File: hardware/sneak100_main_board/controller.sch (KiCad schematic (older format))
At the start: 17 parts, among them U7 STM32F405RGTx, Y1 8MHz

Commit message: Hardware configuration schematic
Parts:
- added R24, R25: 4k7, Resistor_SMD:R_0805_2012Metric, symbol Device:R
- renumbered C13 to C14, C14 to C15, C15 to C16, C16 to C17, C17 to C18, C18 to C19, C19 to C20, C20 to C21, C21 to C22, C22 to C23, C23 to C24, C24 to C25, R19 to R23, U7 to U8
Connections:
- net +3V3: now also R24.1, R25.1
- net LINE_RM: now reaches U8.10 (PC2)
- net LINE_RR: now reaches U8.11 (PC3)
- net RF_A: now reaches U8.14 (PA0)
- net RF_B: now reaches U8.15 (PA1)
- net USART2_TX: now reaches U8.16 (PA2)
- net USART2_RX: now reaches U8.17 (PA3)
- net MODULE_START: now reaches U8.2 (PC13)
- net LB_A: now reaches U8.22 (PA6)
- net LB_B: now reaches U8.23 (PA7)
- net BATTERY_SENSE: now reaches U8.24 (PC4)
- net PROXIMITY_RX_READ: now reaches U8.25 (PC5)
- net LB_IN1: now reaches U8.26 (PB0)
- net LB_IN2: now reaches U8.27 (PB1)
- net RF_IN1: now reaches U8.29 (PB10)
- net MODULE_KILL: now reaches U8.3 (PC14)
- net RF_IN2: now reaches U8.30 (PB11)
- net LF_IN1: now reaches U8.35 (PB14)
- net LF_IN2: now reaches U8.36 (PB15)
- net LF_A: now reaches U8.37 (PC6)
- net LF_B: now reaches U8.38 (PC7)
- net PROXIMITY_TX_ENABLE: now reaches U8.39 (PC8)
- net I2C3_SDA: now reaches U8.40 (PC9)
- net I2C3_SDA: now also R25.2
- net I2C3_SCL: now reaches U8.41 (PA8)
- net I2C3_SCL: now also R24.2
- net USB_DM: now reaches U8.44 (PA11)
- net USB_DP: now reaches U8.45 (PA12)
- net USER_LED1: now reaches U8.50 (PA15)
- net USER_LED2: now reaches U8.51 (PC10)
- net USER_LED3: now reaches U8.52 (PC11)
- net USER_BUTTON: now reaches U8.53 (PC12)
- net RECEIVER_OUT: now reaches U8.54 (PD2)
- net PROXIMITY_ADD0: now reaches U8.55 (PB3)
- net PROXIMITY_ADD1: now reaches U8.56 (PB4)
- net PROXIMITY_ADD2: now reaches U8.57 (PB5)
- net RB_A: now reaches U8.58 (PB6)
- net RB_B: now reaches U8.59 (PB7)
- net RB_IN1: now reaches U8.61 (PB8)
- net RB_IN2: now reaches U8.62 (PB9)
- net LINE_LL: now reaches U8.8 (PC0)
- net LINE_LM: now reaches U8.9 (PC1)
- no-connect marks 3 -> 11

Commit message: Power section scheme
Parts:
- C18: renamed from C14; footprint Capacitor_SMD:C_0805_2012Metric -> Capacitor_SMD:C_0603_1608Metric
- C19: renamed from C15; footprint Capacitor_SMD:C_0805_2012Metric -> Capacitor_SMD:C_0603_1608Metric
- C20: renamed from C16; footprint Capacitor_SMD:C_0805_2012Metric -> Capacitor_SMD:C_0603_1608Metric
- C21: renamed from C17; footprint Capacitor_SMD:C_0805_2012Metric -> Capacitor_SMD:C_0603_1608Metric
- C22: renamed from C18; footprint Capacitor_SMD:C_0805_2012Metric -> Capacitor_SMD:C_0603_1608Metric
- C23: renamed from C19; footprint Capacitor_SMD:C_0805_2012Metric -> Capacitor_SMD:C_0603_1608Metric
- C24: renamed from C20; footprint Capacitor_SMD:C_0805_2012Metric -> Capacitor_SMD:C_0603_1608Metric
- C25: renamed from C21; footprint Capacitor_SMD:C_0805_2012Metric -> Capacitor_SMD:C_0603_1608Metric
- C26: renamed from C22; footprint Capacitor_SMD:C_0805_2012Metric -> Capacitor_SMD:C_0603_1608Metric
- C27: renamed from C23; footprint Capacitor_SMD:C_0805_2012Metric -> Capacitor_SMD:C_0603_1608Metric
- C28: renamed from C24; footprint Capacitor_SMD:C_0805_2012Metric -> Capacitor_SMD:C_0603_1608Metric
- renumbered C25 to C29, R23 to R32, R24 to R33, R25 to R34, U8 to U9

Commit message: USB FDU mode
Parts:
- added R19: 4k7, Resistor_SMD:R_0603_1608Metric, symbol Device:R
- added SW2: SW_SPST, Button_Switch_THT:SW_DIP_SPSTx01_Slide_9.78x4.72mm_W7.62mm_P2.54mm, symbol Switch:SW_SPST
- added SW5: SW_Push, Button_Switch_SMD:SW_SPST_FSMSM, symbol Switch:SW_Push
- R20: renamed from R32; value 10k -> 4k7; footprint Resistor_SMD:R_0805_2012Metric -> Resistor_SMD:R_0603_1608Metric
- R21: renamed from R33; footprint Resistor_SMD:R_0805_2012Metric -> Resistor_SMD:R_0603_1608Metric
- R22: renamed from R34; footprint Resistor_SMD:R_0805_2012Metric -> Resistor_SMD:R_0603_1608Metric
- renumbered C18 to C16, C19 to C17, C20 to C18, C21 to C19, C22 to C20, C23 to C21, C24 to C22, C25 to C23, C26 to C24, C27 to C25, C28 to C26, C29 to C27, U9 to U8
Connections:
- net labels added: BOOT0, BOOT1
- wire segments 37 -> 46
- no-connect marks 11 -> 10

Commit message: Layout progress
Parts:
- removed C16: 100nF, Capacitor_SMD:C_0603_1608Metric, symbol Device:C
- removed SW2: SW_SPST, Button_Switch_THT:SW_DIP_SPSTx01_Slide_9.78x4.72mm_W7.62mm_P2.54mm, symbol Switch:SW_SPST
- removed SW5: SW_Push, Button_Switch_SMD:SW_SPST_FSMSM, symbol Switch:SW_Push
- added J14: Conn_02x02_Odd_Even, Connector_PinHeader_2.54mm:PinHeader_2x02_P2.54mm_Vertical, symbol Connector_Generic:Conn_02x02_Odd_Even
- renumbered C17 to C18, C18 to C19, C19 to C20, C20 to C21, C21 to C22, C22 to C23, C23 to C24, C24 to C25, C25 to C26, C26 to C27, C27 to C28, R19 to R27, R20 to R28, R21 to R29, R22 to R30, U8 to U9
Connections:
- net labels added: RST, ST-LINK_3.3V
- net labels removed: MODULE_KILL, MODULE_START, RESET
- wire segments 46 -> 40
- no-connect marks 10 -> 12
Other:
- moved on the sheet: R27, R28

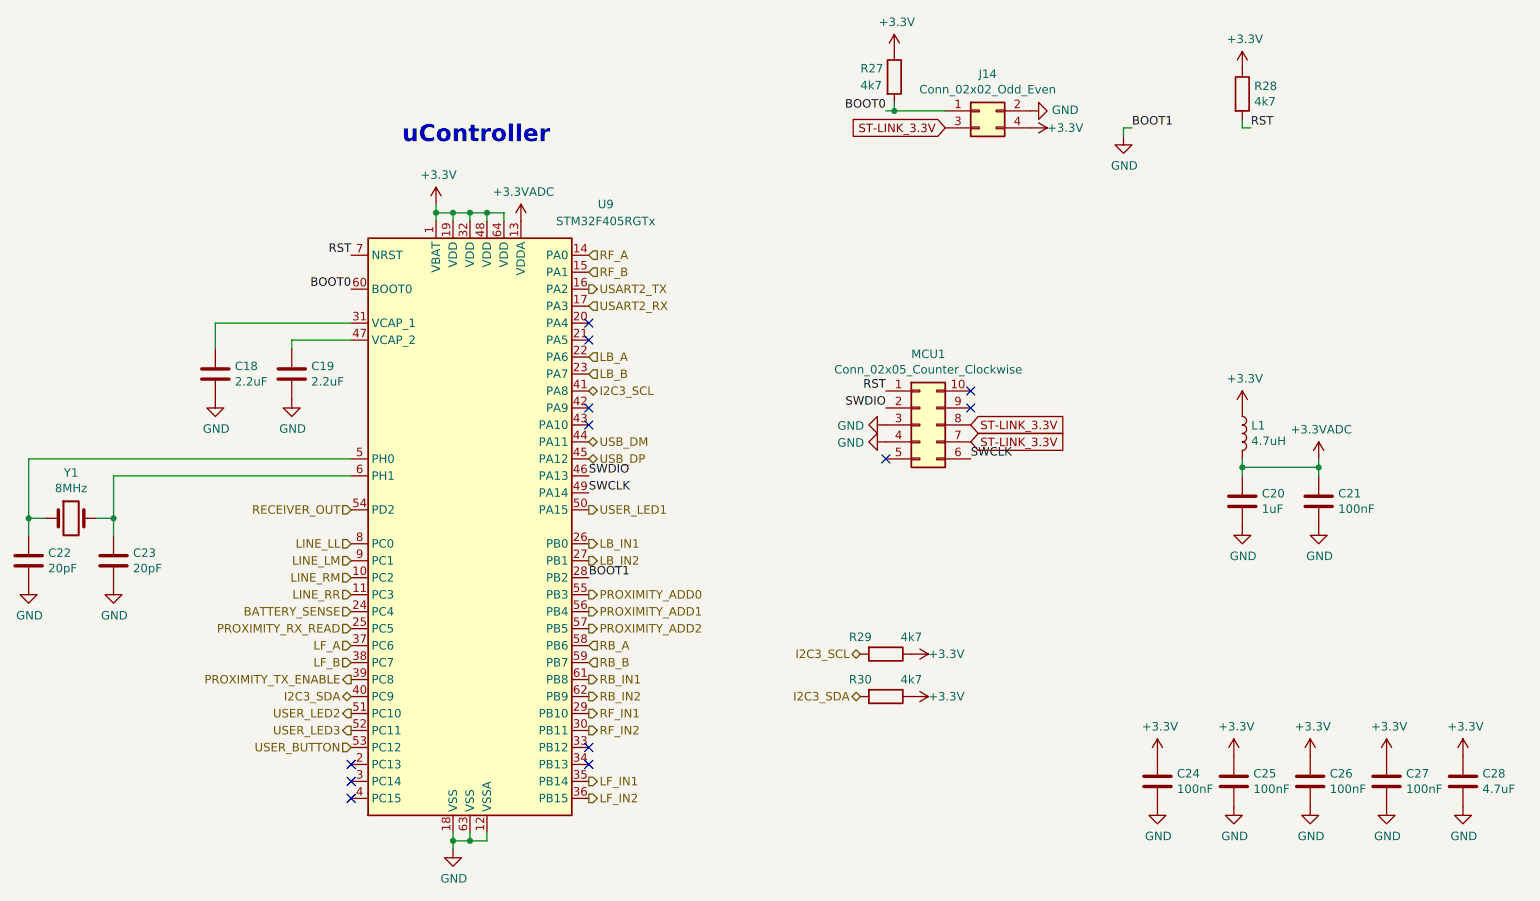
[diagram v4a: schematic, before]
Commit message: Add OLED display
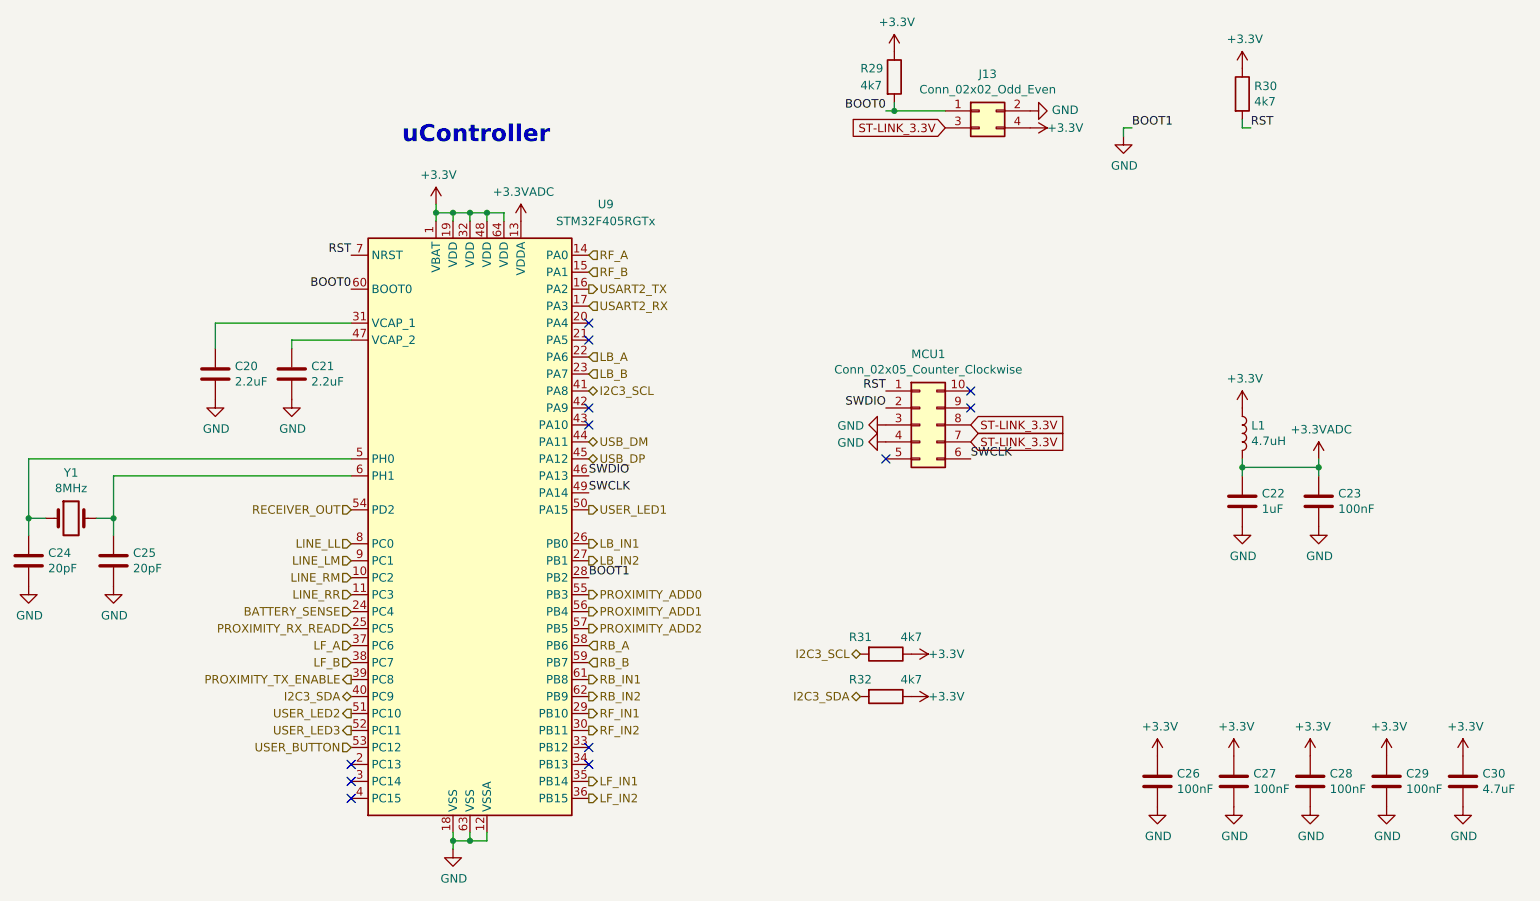
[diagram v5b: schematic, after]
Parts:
- renumbered C18 to C20, C19 to C21, C20 to C22, C21 to C23, C22 to C24, C23 to C25, C24 to C26, C25 to C27, C26 to C28, C27 to C29, C28 to C30, J14 to J13, R27 to R29, R28 to R30, R29 to R31, R30 to R32

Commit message: delete USB, modify top hull, bigger PCB board
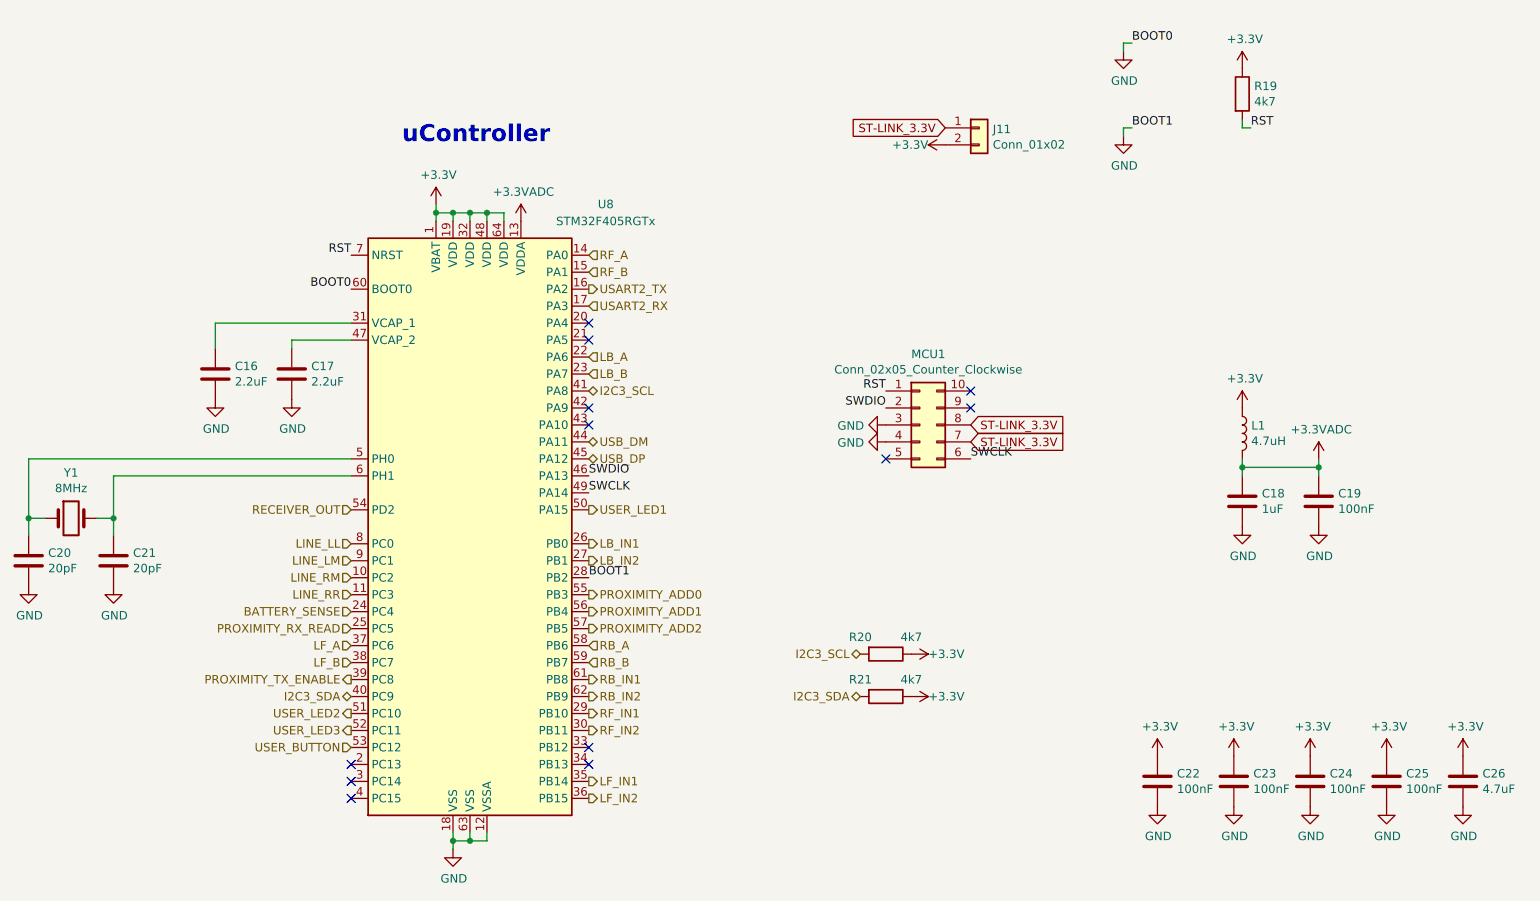
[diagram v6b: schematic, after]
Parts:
- removed J13: Conn_02x02_Odd_Even, Connector_PinHeader_2.54mm:PinHeader_2x02_P2.54mm_Vertical, symbol Connector_Generic:Conn_02x02_Odd_Even
- removed R29: 4k7, Resistor_SMD:R_0603_1608Metric, symbol Device:R
- added J11: Conn_01x02, Connector_PinHeader_2.54mm:PinHeader_1x02_P2.54mm_Vertical, symbol Connector_Generic:Conn_01x02
- renumbered C20 to C16, C21 to C17, C22 to C18, C23 to C19, C24 to C20, C25 to C21, C26 to C22, C27 to C23, C28 to C24, C29 to C25, C30 to C26, R30 to R19, R31 to R20, R32 to R21, U9 to U8
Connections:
- net BOOT0 is gone; now on net GND: U8.60 (BOOT0)
- net +3V3: now also J11.2 (Pin_2)
- net ST-LINK_3.3V: now also J11.1 (Pin_1)

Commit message: Board interface layout
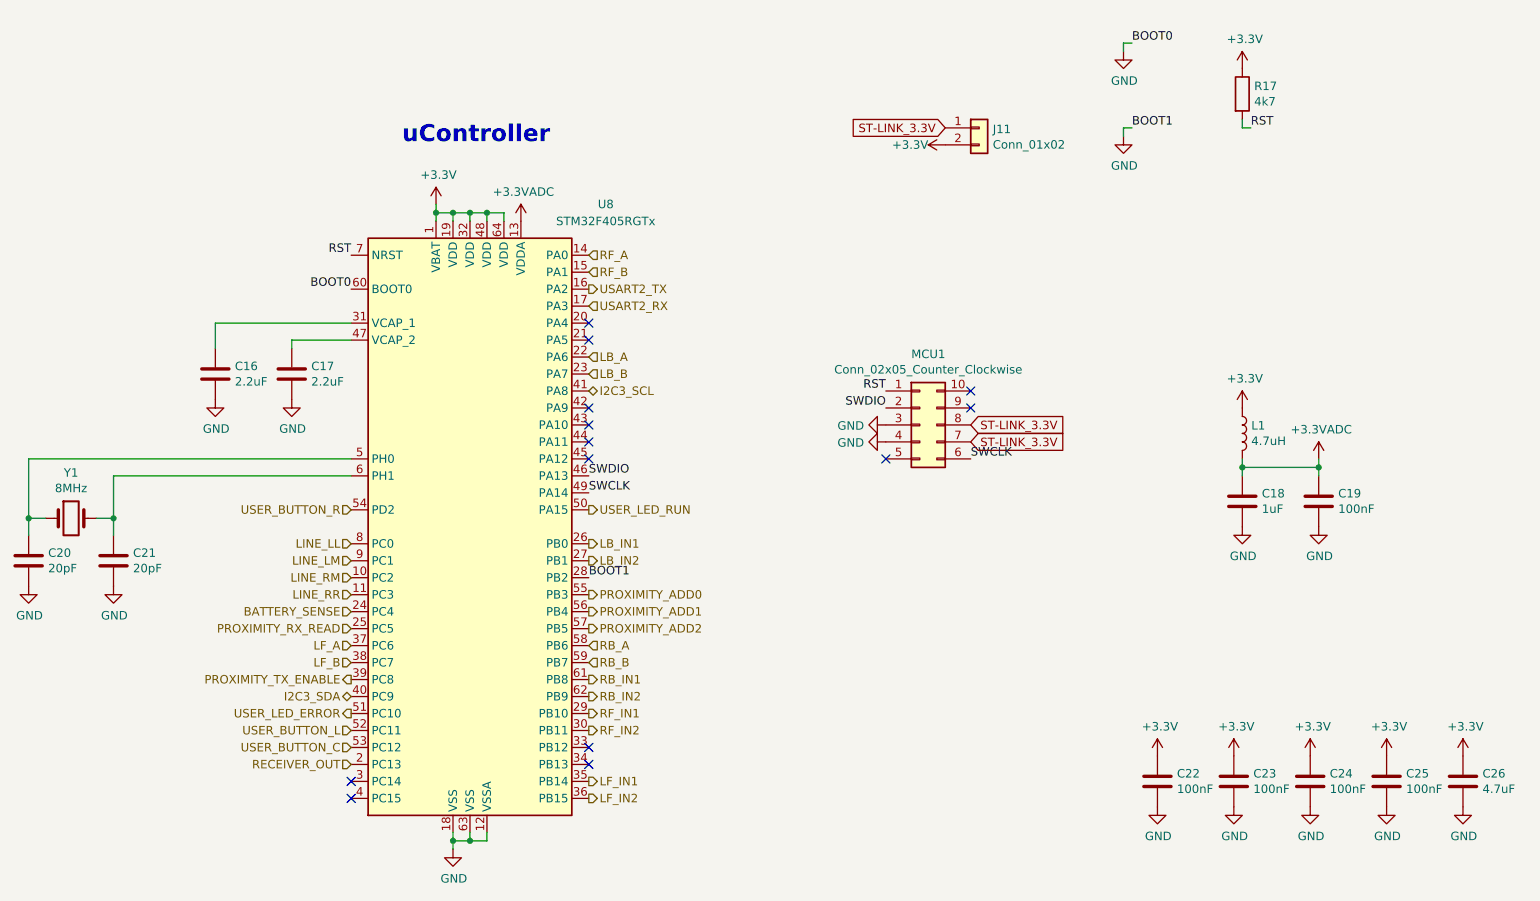
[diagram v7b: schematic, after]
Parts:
- removed R20, R21: 4k7, Resistor_SMD:R_0603_1608Metric, symbol Device:R
- renumbered R19 to R17
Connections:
- net RECEIVER_OUT: now also U8.2 (PC13); no longer U8.54 (PD2)
- net USB_DM: no longer names the net of U8.44 (PA11)
- net USB_DP: no longer names the net of U8.45 (PA12)
- net USER_BUTTON renamed USER_BUTTON_C
- net USER_LED1 renamed USER_LED_RUN
- net USER_LED2 renamed USER_LED_ERROR
- net USER_LED3 renamed USER_BUTTON_L
- new net USER_BUTTON_R: U8.54 (PD2)
- no-connect marks 12 -> 13

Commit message: PCB first full layout
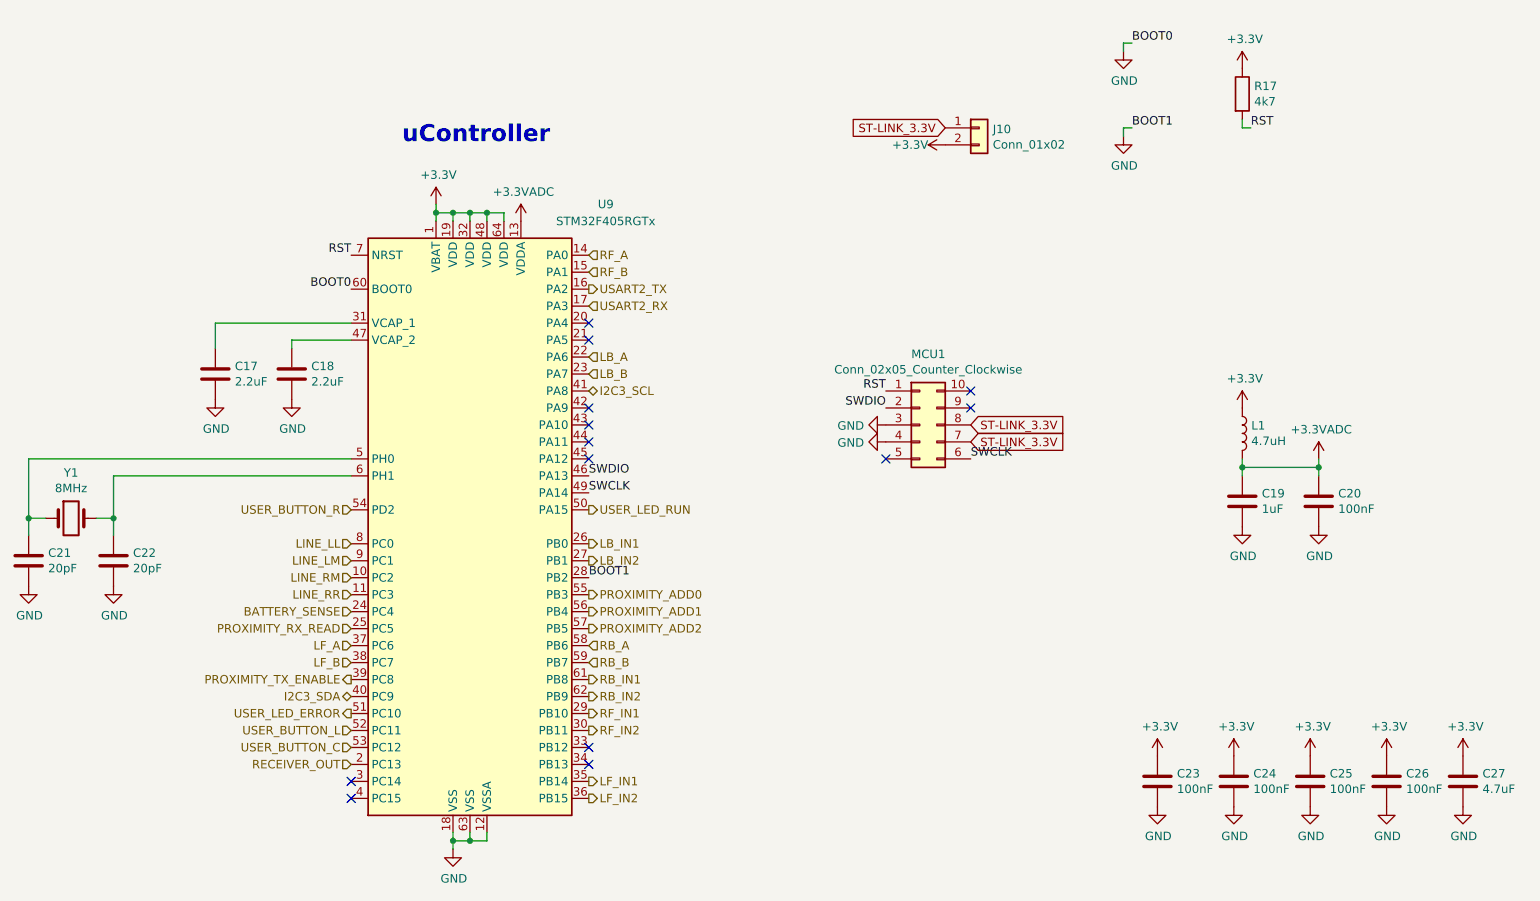
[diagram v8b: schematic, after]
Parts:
- renumbered C16 to C17, C17 to C18, C18 to C19, C19 to C20, C20 to C21, C21 to C22, C22 to C23, C23 to C24, C24 to C25, C25 to C26, C26 to C27, J11 to J10, U8 to U9
